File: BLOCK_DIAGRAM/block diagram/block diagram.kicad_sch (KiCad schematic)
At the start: 0 parts

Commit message: sunday - simplified block
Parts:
- added BZ1: Buzzer, symbol Device:Buzzer
- added C1: C, symbol Device:C
- added Q1: NMOS, symbol Simulation_SPICE:NMOS
- added R1, R2: 10k, symbol Device:R
- added R3, R4, R5, R6: R, symbol Device:R
- added U1: ESP32-C3-WROOM-02, RF_Module:ESP32-C3-WROOM-02, symbol RF_Module:ESP32-C3-WROOM-02
- added U2: STM8S003F3P, Package_SO:TSSOP-20_4.4x6.5mm_P0.65mm, symbol MCU_ST_STM8:STM8S003F3P
- added U3: MQ-4M, Sensor:MQ-6, symbol Sensor_Gas:MQ-6
- added U4: 5-3v3, Sensor:MQ-6, symbol Sensor_Gas:MQ-6
- added U5: 12-5v, Sensor:MQ-6, symbol Sensor_Gas:MQ-6
- added U6: 220-12v, Sensor:MQ-6, symbol Sensor_Gas:MQ-6
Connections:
- new net: U5.1 (12v), U6.2 (12v)
- new net: BZ1.1 (+), R2.1, U2.9 (VDD), U4.1 (5v), U5.2 (5v)
- new net: U2.14 (PC4), U3.1 (A_O)
- new net: R1.1, U1.1 (3V3), U3.3 (VCC), U4.2 (3v3)
- new net: C1.1, U2.8 (VCAP)
- new net: BZ1.2 (-), Q1.1 (D)
- new net: Q1.2 (G), R3.1
- new net: Q1.3 (S), R4.1
- new net: R1.2, U1.16 (IO2), U1.7 (IO8), U1.8 (IO9)
- new net: R2.2, U2.4 (NRST)
- new net: U1.2 (EN), U2.10 (PA3)
- new net: U1.5 (IO6), U2.15 (PC5)
- new net: R5.1, U2.2 (PD5)
- new net: R6.1, U2.3 (PD6)
- new net: R3.2, U2.5 (PA1)
- new net: R6.2, U1.12 (IO21/TXD)
- new net: R5.2, U1.11 (IO20/RXD)
- new net GND: C1.2, R4.2, U1.19 (GND), U1.9 (GND), U2.7 (VSS), U3.4 (GND)
- no-connect marks 0 -> 1

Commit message: monday - start of prototype simplified schematic
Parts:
- removed BZ1: Buzzer, symbol Device:Buzzer
- removed C1: C, symbol Device:C
- removed Q1: NMOS, symbol Simulation_SPICE:NMOS
- removed R1, R2: 10k, symbol Device:R
- removed R3, R4, R5, R6: R, symbol Device:R
- removed U1: ESP32-C3-WROOM-02, RF_Module:ESP32-C3-WROOM-02, symbol RF_Module:ESP32-C3-WROOM-02
- removed U2: STM8S003F3P, Package_SO:TSSOP-20_4.4x6.5mm_P0.65mm, symbol MCU_ST_STM8:STM8S003F3P
- removed U3: MQ-4M, Sensor:MQ-6, symbol Sensor_Gas:MQ-6
- removed U4: 5-3v3, Sensor:MQ-6, symbol Sensor_Gas:MQ-6
- removed U5: 12-5v, Sensor:MQ-6, symbol Sensor_Gas:MQ-6
- removed U6: 220-12v, Sensor:MQ-6, symbol Sensor_Gas:MQ-6
- added BZ2: Buzzer, symbol Device:Buzzer
- added C2: 10nF, symbol Device:C
- added C3: 1uF, symbol Device:C
- added D1: SK6812, LED_SMD:LED_SK6812_PLCC4_5.0x5.0mm_P3.2mm, symbol LED:SK6812
- added PS1: HLK-5M05, Converter_ACDC:Converter_ACDC_Hi-Link_HLK-5Mxx, symbol Converter_ACDC:HLK-5M05
- added Q2, Q3: NMOS, symbol Simulation_SPICE:NMOS
- added R7, R8: 10k, symbol Device:R
- added R9: 100, symbol Device:R
- added U10: AMS1117-3.3, Package_TO_SOT_SMD:SOT-223-3_TabPin2, symbol Regulator_Linear:AMS1117-3.3
- added U11: ESP32-WROOM-32E, RF_Module:ESP32-WROOM-32D, symbol RF_Module:ESP32-WROOM-32E
- added U8: CI121S021 [adc], Package_TO_SOT_SMD:SOT-23-6, symbol Analog_ADC:ADS1110
- added U9: MQ-4M, Sensor:MQ-6, symbol Sensor_Gas:MQ-6
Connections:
- net GND: now also C2.2, C3.2, PS1.3 (-Vout), Q2.3 (S), U10.1 (GND), U11.1 (GND), U11.15 (GND), U11.38 (GND), U11.39 (GND), U8.2 (GND), U9.4 (GND)
- new net: Q2.2 (G), R9.1
- new net: R9.2, U11.10 (IO25)
- new net: BZ2.1 (+), C2.1, C3.1, PS1.4 (+Vout), U10.3 (VI), U8.1 (VA), U9.3 (VCC)
- new net: R7.1, U8.5 (SDATA)
- new net: Q3.1 (D), R7.2
- new net: Q3.2 (G), U10.2 (VO), U11.2 (VDD)
- new net: Q3.3 (S), R8.2
- new net: R8.1, U11.28 (IO17)
- new net: BZ2.2 (-), Q2.1 (D)
- new net: U8.3 (VIN), U9.1 (A_O)
- new net: U11.30 (IO18), U8.4 (SCLK)
- new net 220V: PS1.1 (AC/L)
- no-connect marks 1 -> 2
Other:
- added sheet old schem (untitled.kicad_sch)
- added sheet sensor module (sensor_mod.kicad_sch)

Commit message: added to do list
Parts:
- added J1: Conn_01x06_Pin, symbol Connector:Conn_01x06_Pin
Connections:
- net GND: now also J1.6 (Pin_6)
- net at Q3.2 (G), U10.2 (VO), U11.2 (VDD): now also J1.1 (Pin_1)
- net at U11.25 (IO0): now also J1.3 (Pin_3)
- net at U11.3 (EN): now also J1.2 (Pin_2)
- net at U11.34 (RXD0/IO3): now also J1.5 (Pin_5)
- net at U11.35 (TXD0/IO1): now also J1.4 (Pin_4)
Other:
- note added: "to do: - add resistors and capacators - check EN pullup (maybe add on/off switch?) - LED indicating on - LED indicating gas detected - do the proper connections for the 220-5v - create module for sensor"
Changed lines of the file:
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@@
 	(generator_version "9.0")
 	(paper "A4")
+	(text "to do:\n- add resistors and capacators\n- check EN pullup (maybe add on/off switch?)\n- LED indicating on\n- LED indicating gas detected\n- do the proper connections for the 220-5v\n- create module for sensor\n"
+		(exclude_from_sim no)
+		(at 37.338 103.886 0)
+		(effects
+			(font
+				(size 2 2)
+				(thickness 0.4)
+				(bold yes)
+			)
+			(justify left)
+		)
+	)
 	(junction
 		(at 114.3 62.23)
@@
 	)
 	(junction
+		(at 222.25 99.06)
+		(diameter 0)
+		(color 0 0 0 0)
+	)
+	(junction
 		(at 114.3 83.82)
 		(diameter 0)
@@
 	)
 	(junction
+		(at 195.58 16.51)
+		(diameter 0)
+		(color 0 0 0 0)
+	)
+	(junction
 		(at 114.3 54.61)
 		(diameter 0)
@@
 	(wire
 		(pts
+			(xy 195.58 16.51) (xy 195.58 24.13)
+		)
+		(stroke
+			(width 0)
+			(type default)
+		)
+	)
+	(wire
+		(pts
 			(xy 53.34 63.5) (xy 53.34 83.82)
 		)
@@
 	(wire
 		(pts
+			(xy 195.58 26.67) (xy 196.85 26.67)
+		)
+		(stroke
+			(width 0)
+			(type default)
+		)
+	)
+	(wire
+		(pts
+			(xy 222.25 99.06) (xy 222.25 114.3)
+		)
+		(stroke
+			(width 0)
+			(type default)
+		)
+	)
+	(wire
+		(pts
 			(xy 114.3 114.3) (xy 114.3 118.11)
 		)
@@
 	(wire
 		(pts
+			(xy 207.01 36.83) (xy 200.66 36.83)
+		)
+		(stroke
+			(width 0)
+			(type default)
+		)
+	)
+	(wire
+		(pts
+			(xy 200.66 36.83) (xy 200.66 34.29)
+		)
+		(stroke
+			(width 0)
+			(type default)
+		)
+	)
+	(wire
+		(pts
+			(xy 198.12 36.83) (xy 198.12 99.06)
+		)
+		(stroke
+			(width 0)
+			(type default)
+		)
+	)
+	(wire
+		(pts
+			(xy 237.49 29.21) (xy 237.49 25.4)
+		)
+		(stroke
+			(width 0)
+			(type default)
+		)
+	)
+	(wire
+		(pts
 			(xy 33.02 58.42) (xy 25.4 58.42)
 		)
@@
 	(wire
 		(pts
-			(xy 222.25 95.25) (xy 222.25 114.3)
+			(xy 222.25 95.25) (xy 222.25 99.06)
+		)
+		(stroke
+			(width 0)
+			(type default)
+		)
+	)
+	(wire
+		(pts
+			(xy 198.12 99.06) (xy 222.25 99.06)
 		)
 		(stroke
@@
 	(wire
 		(pts
+			(xy 196.85 25.4) (xy 196.85 26.67)
+		)
+		(stroke
+			(width 0)
+			(type default)
+		)
+	)
+	(wire
+		(pts
 			(xy 109.22 69.85) (xy 109.22 58.42)
 		)
@@
 	(wire
 		(pts
-			(xy 177.8 16.51) (xy 222.25 16.51)
+			(xy 195.58 29.21) (xy 207.01 29.21)
+		)
+		(stroke
+			(width 0)
+			(type default)
+		)
+	)
+	(wire
+		(pts
+			(xy 177.8 16.51) (xy 195.58 16.51)
+		)
+		(stroke
+			(width 0)
+			(type default)
+		)
+	)
+	(wire
+		(pts
+			(xy 195.58 31.75) (xy 207.01 31.75)
+		)
+		(stroke
+			(width 0)
+			(type default)
+		)
+	)
+	(wire
+		(pts
+			(xy 237.49 25.4) (xy 196.85 25.4)
 		)
 		(stroke
@@
 	(wire
 		(pts
+			(xy 200.66 34.29) (xy 195.58 34.29)
+		)
+		(stroke
+			(width 0)
+			(type default)
+		)
+	)
+	(wire
+		(pts
+			(xy 195.58 16.51) (xy 222.25 16.51)
+		)
+		(stroke
+			(width 0)
+			(type default)
+		)
+	)
+	(wire
+		(pts
 			(xy 157.48 86.36) (xy 157.48 67.31)
 		)
@@
 		(pts
 			(xy 130.81 50.8) (xy 130.81 83.82)
+		)
+		(stroke
+			(width 0)
+			(type default)
+		)
+	)
+	(wire
+		(pts
+			(xy 198.12 36.83) (xy 195.58 36.83)
 		)
 		(stroke
@@
 					(unit 1)
 				)
+			)
+		)
+	)
+	(symbol
+		(lib_id "Connector:Conn_01x06_Pin")
+		(at 190.5 29.21 0)
+		(unit 1)
+		(exclude_from_sim no)
+		(in_bom yes)
+		(on_board yes)
+		(dnp no)
+		(property "Reference" "J1"
+			(at 191.135 19.05 0)
+			(effects
+				(font
+					(size 1.27 1.27)
+				)
+			)
+		)
+		(property "Value" "Conn_01x06_Pin"
+			(at 191.135 21.59 0)
+			(effects
+				(font
+					(size 1.27 1.27)
+				)
+			)
+		)
+		(property "Footprint" ""
+			(at 190.5 29.21 0)
+			(effects
+				(font
+					(size 1.27 1.27)
+				)
+				(hide yes)
+			)
+		)
+		(property "Datasheet" "~"
+			(at 190.5 29.21 0)
+			(effects
+				(font
+					(size 1.27 1.27)
+				)
+				(hide yes)
+			)
+		)
+		(property "Description" "Generic connector, single row, 01x06, script generated"
+			(at 190.5 29.21 0)
+			(effects
+				(font
+					(size 1.27 1.27)
+				)
+				(hide yes)
+			)
+		)
+		(pin "1"
+		)
+		(pin "2"
+		)
+		(pin "3"
+		)
+		(pin "4"
+		)
+		(pin "5"
+		)
+		(pin "6"
+		)
+		(instances
+			(project "block diagram"
+				(path "/290c0625-1e23-4ef7-8910-f1eb5378fd87"
+					(reference "J1")
+					(unit 1)
+				)

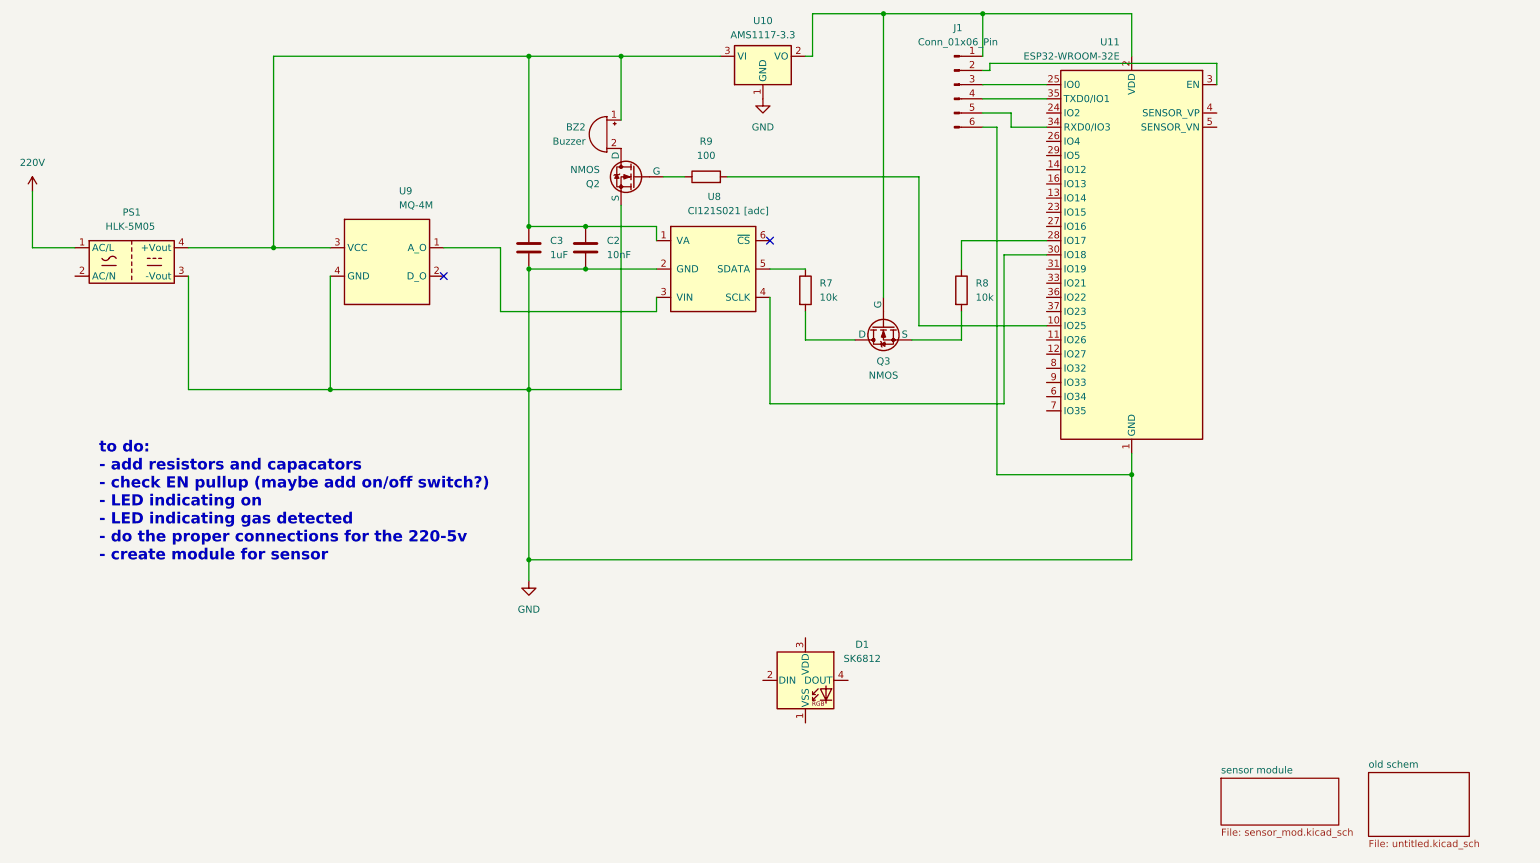
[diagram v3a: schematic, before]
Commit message: edited the connections of the 220-5 (added the RLC) and added RLC for en pullup and 3v3 of esp
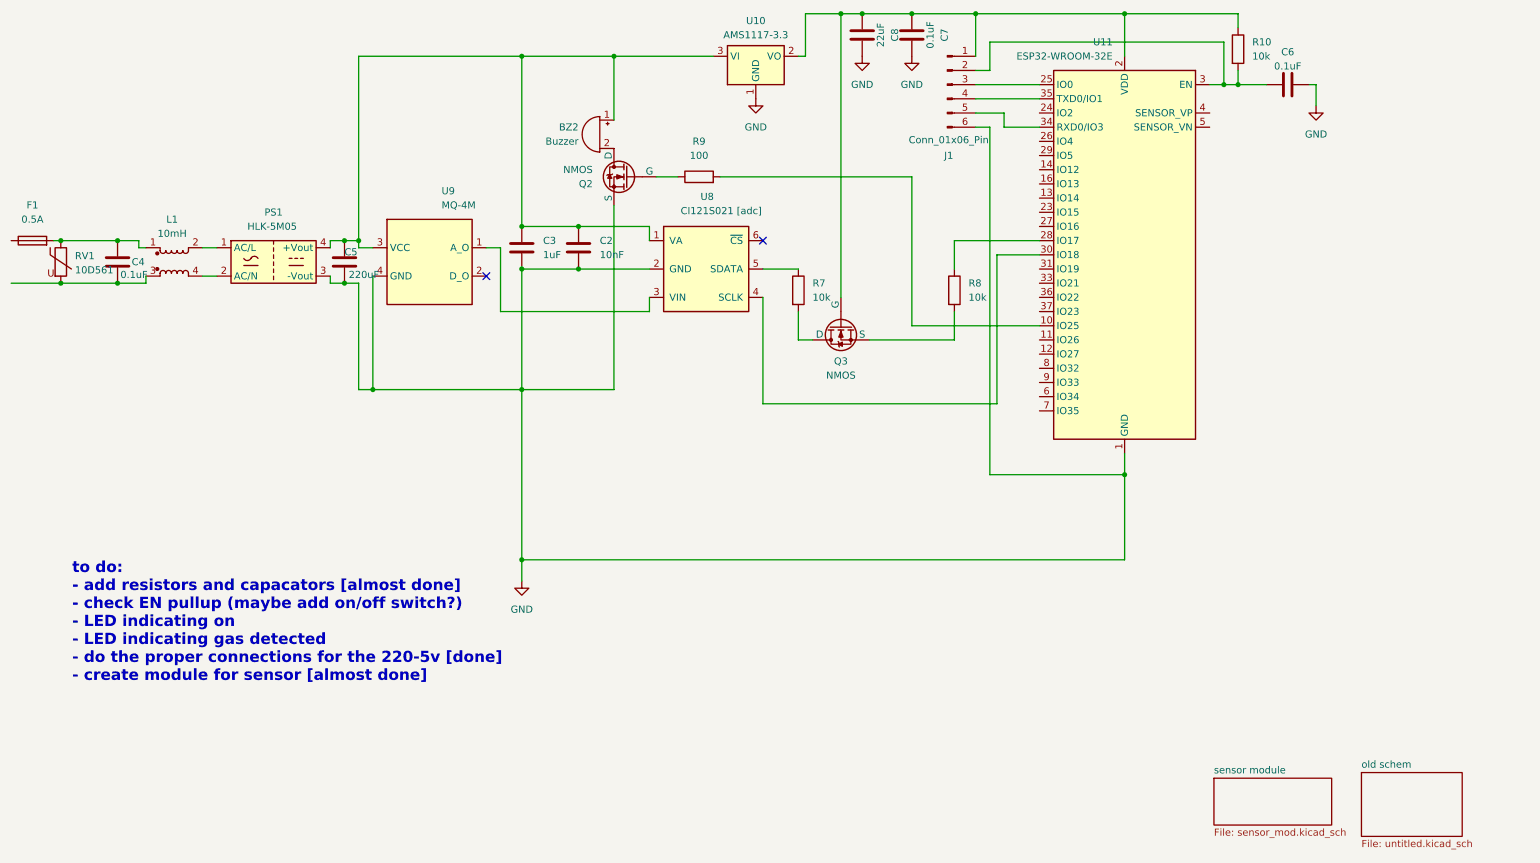
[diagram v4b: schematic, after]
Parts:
- removed D1: SK6812, LED_SMD:LED_SK6812_PLCC4_5.0x5.0mm_P3.2mm, symbol LED:SK6812
- added C4, C6, C7: 0.1uF, symbol Device:C
- added C5: 220uF, symbol Device:C
- added C8: 22uF, symbol Device:C
- added F1: 0.5A, symbol Device:Fuse
- added L1: 10mH, symbol Device:L_Coupled
- added R10: 10k, symbol Device:R
- added RV1: 10D561, symbol Device:Varistor
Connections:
- net GND: now also C5.2, C6.2, C7.2, C8.2
- net at PS1.2 (AC/N): now also L1.4
- net at BZ2.1 (+), C2.1, C3.1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: now also C5.1
- net at J1.1 (Pin_1), Q3.2 (G), U10.2 (VO)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: now also C7.1, C8.1, R10.1
- net at J1.2 (Pin_2), U11.3 (EN): now also C6.1, R10.2
- net 220V: no longer names the net of PS1.1 (AC/L)
- net 220V: now also L1.2
- new net: C4.1, F1.2, L1.1, RV1.1
- new net: C4.2, L1.3, RV1.2
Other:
- note added: "to do: - add resistors and capacators [almost done] - check EN pullup (maybe add on/off switch?) - LED indicating on - LED indicating gas detected - do the proper connections for the 220-5v [done] - create module for sensor [almost done]"
- note removed: "to do: - add resistors and capacators - check EN pullup (maybe add on/off switch?) - LED indicating on - LED indicating gas detected - do the proper connections for the 220-5v - create module for sensor"
- moved on the sheet: BZ2, C2, C3, J1, PS1, Q2, Q3, R7, R8, R9, U10, U11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

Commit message: updated overall schematic, should be done [will be checked]
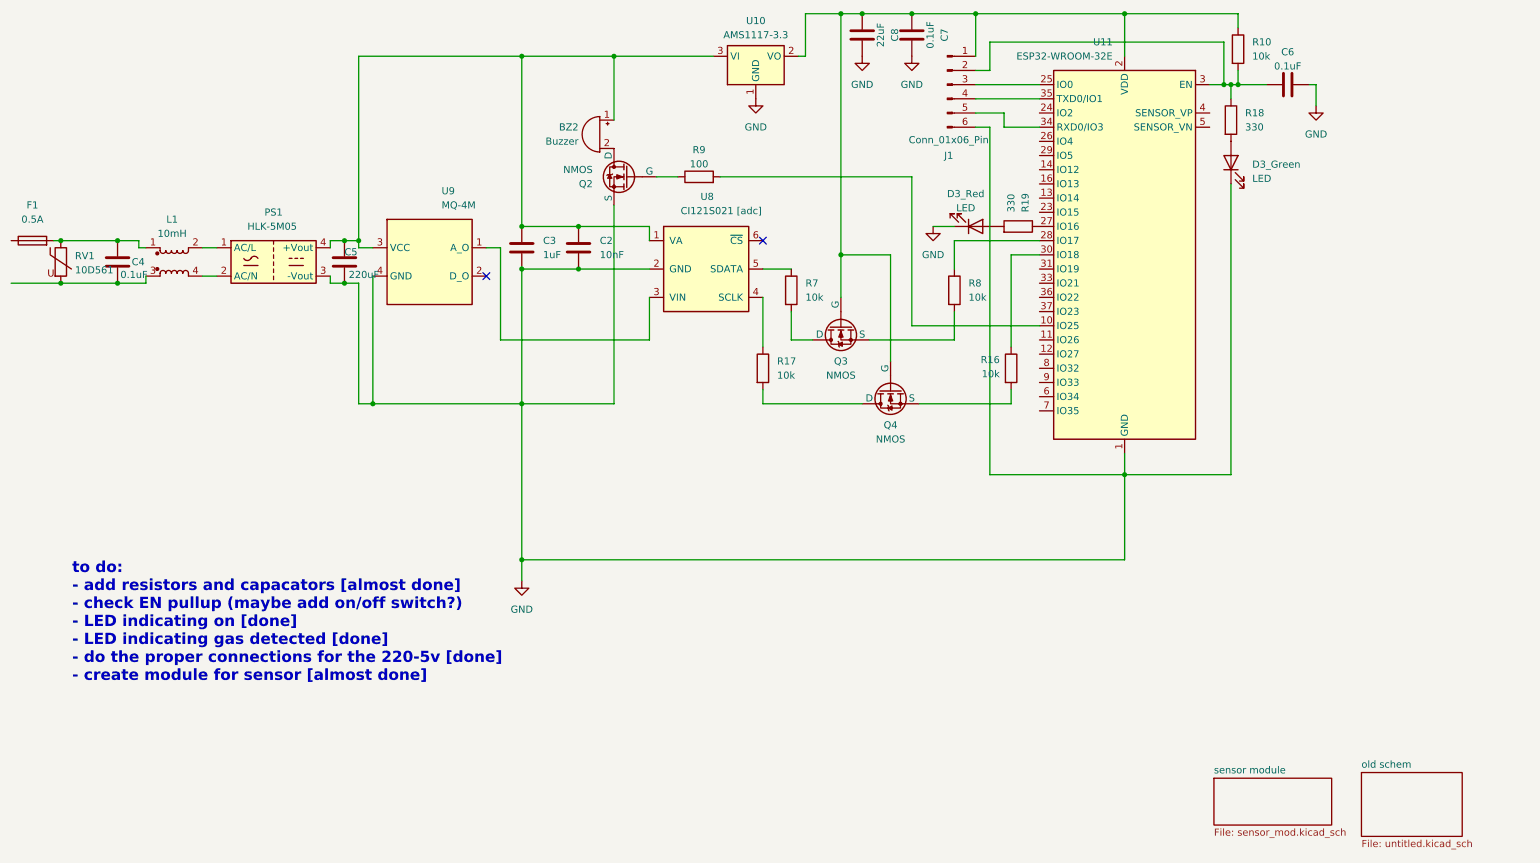
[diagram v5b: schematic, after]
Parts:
- added D3_Green, D3_Red: LED, symbol Device:LED
- added Q4: NMOS, symbol Simulation_SPICE:NMOS
- added R16, R17: 10k, symbol Device:R
- added R18, R19: 330, symbol Device:R
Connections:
- net GND: now also D3_Green.1 (K), D3_Red.1 (K)
- net at C7.1, C8.1, J1.1 (Pin_1)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: now also Q4.2 (G)
- net at C6.1, J1.2 (Pin_2), R10.2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: now also R18.1
- net at U11.30 (IO18): now also R16.1; no longer U8.4 (SCLK)
- net at U11.27 (IO16): now also R19.1
- new net: Q4.3 (S), R16.2
- new net: Q4.1 (D), R17.2
- new net: D3_Green.2 (A), R18.2
- new net: D3_Red.2 (A), R19.2
- new net: R17.1, U8.4 (SCLK)
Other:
- note added: "to do: - add resistors and capacators [almost done] - check EN pullup (maybe add on/off switch?) - LED indicating on [done] - LED indicating gas detected [done] - do the proper connections for the 220-5v [done] - create module for sensor [almost done]"
- note removed: "to do: - add resistors and capacators [almost done] - check EN pullup (maybe add on/off switch?) - LED indicating on - LED indicating gas detected - do the proper connections for the 220-5v [done] - create module for sensor [almost done]"
- moved on the sheet: R7
